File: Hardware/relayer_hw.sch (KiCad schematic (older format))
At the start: 18 parts

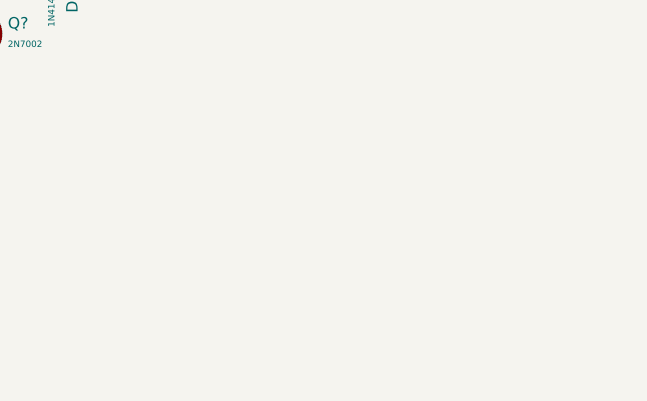
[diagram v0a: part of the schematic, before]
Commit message: Esquematico do regulador linear da fonte
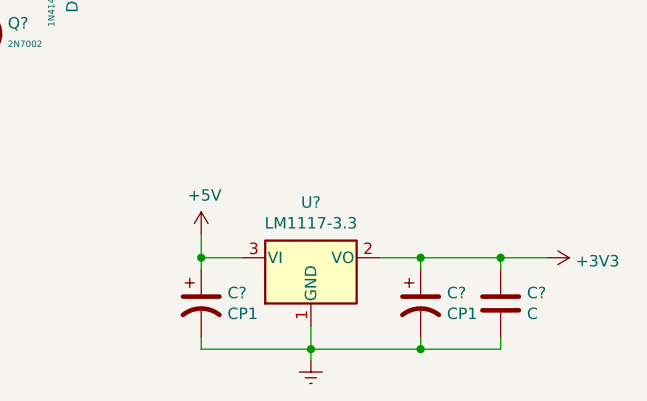
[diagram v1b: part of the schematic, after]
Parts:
- added C? (x2): CP1, symbol Device:CP1
- added C?: C, symbol Device:C
- added U?: LM1117-3.3, symbol Regulator_Linear:LM1117-3.3
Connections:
- wire segments 41 -> 57
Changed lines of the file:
@@
 	3390 5450 3390 5240
 Connection ~ 3390 5240
+$Comp
+L Regulator_Linear:LM1117-3.3 U?
+U 1 1 60667377
+P 3700 6690
+F 0 "U?" H 3700 6932 50  0000 C CNN
+F 1 "LM1117-3.3" H 3700 6841 50  0000 C CNN
+F 2 "" H 3700 6690 50  0001 C CNN
+F 3 "http://www.ti.com/lit/ds/symlink/lm1117.pdf" H 3700 6690 50  0001 C CNN
+	1    3700 6690
+	1    0    0    -1
+$EndComp
+$Comp
+L Device:CP1 C?
+U 1 1 60668957
+P 3220 6890
+F 0 "C?" H 3335 6936 50  0000 L CNN
+F 1 "CP1" H 3335 6845 50  0000 L CNN
+F 2 "" H 3220 6890 50  0001 C CNN
+F 3 "~" H 3220 6890 50  0001 C CNN
+	1    3220 6890
+	1    0    0    -1
+$EndComp
+$Comp
+L Device:CP1 C?
+U 1 1 60669A49
+P 4180 6890
+F 0 "C?" H 4295 6936 50  0000 L CNN
+F 1 "CP1" H 4295 6845 50  0000 L CNN
+F 2 "" H 4180 6890 50  0001 C CNN
+F 3 "~" H 4180 6890 50  0001 C CNN
+	1    4180 6890
+	1    0    0    -1
+$EndComp
+$Comp
+L Device:C C?
+U 1 1 6066C69B
+P 4530 6890
+F 0 "C?" H 4645 6936 50  0000 L CNN
+F 1 "C" H 4645 6845 50  0000 L CNN
+F 2 "" H 4568 6740 50  0001 C CNN
+F 3 "~" H 4530 6890 50  0001 C CNN
+	1    4530 6890
+	1    0    0    -1
+$EndComp
+Wire Wire Line
+	3220 6740 3220 6690
+Wire Wire Line
+	3220 6690 3400 6690
+Wire Wire Line
+	4000 6690 4180 6690
+Wire Wire Line
+	4180 6690 4180 6740
+Wire Wire Line
+	4530 6740 4530 6690
+Wire Wire Line
+	4530 6690 4180 6690
+Connection ~ 4180 6690
+Wire Wire Line
+	3220 7040 3220 7090
+Wire Wire Line
+	3220 7090 3700 7090
+Wire Wire Line
+	4180 7090 4180 7040
+Wire Wire Line
+	4530 7040 4530 7090
+Wire Wire Line
+	4530 7090 4180 7090
+Connection ~ 4180 7090
+Wire Wire Line
+	3700 6990 3700 7090
+Connection ~ 3700 7090
+Wire Wire Line
+	3700 7090 4180 7090
+$Comp
+L power:Earth #PWR?
+U 1 1 60672AE5
+P 3700 7140
+F 0 "#PWR?" H 3700 6890 50  0001 C CNN
+F 1 "Earth" H 3700 6990 50  0001 C CNN
+F 2 "" H 3700 7140 50  0001 C CNN
+F 3 "~" H 3700 7140 50  0001 C CNN
+	1    3700 7140
+	1    0    0    -1
+$EndComp
+Wire Wire Line
+	3700 7140 3700 7090
+$Comp
+L power:+3V3 #PWR?
+U 1 1 60674258
+P 4730 6690
+F 0 "#PWR?" H 4730 6540 50  0001 C CNN
+F 1 "+3V3" V 4745 6818 50  0000 L CNN
+F 2 "" H 4730 6690 50  0001 C CNN
+F 3 "" H 4730 6690 50  0001 C CNN
+	1    4730 6690
+	0    1    1    0
+$EndComp
+Wire Wire Line
+	4730 6690 4530 6690
+Connection ~ 4530 6690
+$Comp
+L power:+5V #PWR?
+U 1 1 60676AA9
+P 3220 6590
+F 0 "#PWR?" H 3220 6440 50  0001 C CNN
+F 1 "+5V" H 3235 6763 50  0000 C CNN
+F 2 "" H 3220 6590 50  0001 C CNN
+F 3 "" H 3220 6590 50  0001 C CNN
+	1    3220 6590
+	1    0    0    -1
+$EndComp
+Wire Wire Line
+	3220 6590 3220 6690
+Connection ~ 3220 6690
 $EndSCHEMATC

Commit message: Esquematico da fonte (não definitivo)
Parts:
- added C?: 220μF, symbol Device:CP1
- added C?: 100nF/275V, symbol Device:C
- added F?: Fuse, symbol Device:Fuse
- added L?: 10mH, symbol Device:L_Core_Iron_Coupled_Small
- added PS?: HLK-2M05, symbol Usr_Sym:HLK-2M05
- added RV?: Varistor_US, symbol Device:Varistor_US
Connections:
- wire segments 57 -> 68
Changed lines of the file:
@@
 L power:+3V3 #PWR?
 U 1 1 60674258
-P 4730 6690
-F 0 "#PWR?" H 4730 6540 50  0001 C CNN
-F 1 "+3V3" V 4745 6818 50  0000 L CNN
-F 2 "" H 4730 6690 50  0001 C CNN
-F 3 "" H 4730 6690 50  0001 C CNN
-	1    4730 6690
-	0    1    1    0
+P 4730 6590
+F 0 "#PWR?" H 4730 6440 50  0001 C CNN
+F 1 "+3V3" V 4745 6718 50  0000 L CNN
+F 2 "" H 4730 6590 50  0001 C CNN
+F 3 "" H 4730 6590 50  0001 C CNN
+	1    4730 6590
+	1    0    0    -1
 $EndComp
-Wire Wire Line
-	4730 6690 4530 6690
-Connection ~ 4530 6690
 $Comp
 L power:+5V #PWR?
@@
 	3220 6590 3220 6690
 Connection ~ 3220 6690
+$Comp
+L Usr_Sym:HLK-2M05 PS?
+U 1 1 60684E63
+P 2180 6870
+F 0 "PS?" H 2180 7175 50  0000 C CNN
+F 1 "HLK-2M05" H 2180 7084 50  0000 C CNN
+F 2 "" H 2180 7040 50  0001 C CNN
+F 3 "" H 2180 7040 50  0001 C CNN
+	1    2180 6870
+	1    0    0    -1
+$EndComp
+$Comp
+L Device:Fuse F?
+U 1 1 606867F7
+P 1000 6690
+F 0 "F?" V 803 6690 50  0000 C CNN
+F 1 "Fuse" V 894 6690 50  0000 C CNN
+F 2 "" V 930 6690 50  0001 C CNN
+F 3 "~" H 1000 6690 50  0001 C CNN
+	1    1000 6690
+	0    1    1    0
+$EndComp
+$Comp
+L Device:Varistor_US RV?
+U 1 1 60690A8A
+P 1220 6890
+F 0 "RV?" H 1323 6936 50  0000 L CNN
+F 1 "Varistor_US" H 1323 6845 50  0001 L CNN
+F 2 "" V 1150 6890 50  0001 C CNN
+F 3 "~" H 1220 6890 50  0001 C CNN
+	1    1220 6890
+	1    0    0    -1
+$EndComp
+$Comp
+L Device:CP1 C?
+U 1 1 606918D0
+P 2770 6890
+F 0 "C?" H 2885 6936 50  0000 L CNN
+F 1 "220μF" H 2885 6845 50  0000 L CNN
+F 2 "" H 2770 6890 50  0001 C CNN
+F 3 "~" H 2770 6890 50  0001 C CNN
+	1    2770 6890
+	1    0    0    -1
+$EndComp
+$Comp
+L Device:C C?
+U 1 1 60693778
+P 1550 6890
+F 0 "C?" H 1665 6936 50  0000 L CNN
+F 1 "100nF/275V" H 1665 6845 50  0001 L CNN
+F 2 "" H 1588 6740 50  0001 C CNN
+F 3 "~" H 1550 6890 50  0001 C CNN
+	1    1550 6890
+	1    0    0    -1
+$EndComp
+Wire Wire Line
+	2770 7040 2770 7090
+Wire Wire Line
+	2770 7090 3220 7090
+Connection ~ 3220 7090
+Wire Wire Line
+	2770 6740 2770 6690
+Wire Wire Line
+	2770 6690 3220 6690
+Wire Wire Line
+	2580 6790 2610 6790
+Wire Wire Line
+	2610 6790 2610 6690
+Wire Wire Line
+	2610 6690 2770 6690
+Connection ~ 2770 6690
+Wire Wire Line
+	2580 6990 2610 6990
+Wire Wire Line
+	2610 6990 2610 7090
+Wire Wire Line
+	2610 7090 2770 7090
+Connection ~ 2770 7090
+$Comp
+L Device:L_Core_Iron_Coupled_Small L?
+U 1 1 606BC58F
+P 1430 7580
+F 0 "L?" H 1430 7811 50  0000 C CNN
+F 1 "10mH" H 1430 7720 50  0000 C CNN
+F 2 "" H 1430 7580 50  0001 C CNN
+F 3 "~" H 1430 7580 50  0001 C CNN
+	1    1430 7580
+	1    0    0    -1
+$EndComp
+Wire Wire Line
+	4730 6590 4730 6690
+Wire Wire Line
+	4730 6690 4530 6690
+Connection ~ 4530 6690
 $EndSCHEMATC

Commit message: Simbolo do STM32WB55 e alimentação do chip (inicio)
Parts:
- added C?: 10μF, symbol Device:CP1
- added C?: 22μF, symbol Device:CP1
- added C? (x5): 100nF, symbol Device:C
- added C?: 220μF, symbol Device:CP1
- added C?: 100nF/275V, symbol Device:C
- added C? (x2): C, symbol Device:C
- added C? (x2): 4.7μF, symbol Device:C
- added F?: Fuse, symbol Device:Fuse
- added J? (x2): AC_IN, symbol Connector:Screw_Terminal_01x02
- added J?: AC_OUT, symbol Connector:Screw_Terminal_01x02
- added L?: 10mH, symbol Device:L_Core_Iron_Coupled_Small
- added PS?: HLK-2M05, symbol Usr_Sym:HLK-2M05
- added RV?: Varistor_US, symbol Device:Varistor_US
- added U?: LM1117-3.3, symbol Regulator_Linear:LM1117-3.3
- added U?: STM32WB55, symbol Usr_Sym:STM32WB55
- C?: value CP1 -> 10μF
- C?: value CP1 -> 22μF
- C?: value C -> 100nF
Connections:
- net labels added: GNDPWR, VDD, VDDSMPS, VFBSMPS, VLXSMPS
- wire segments 68 -> 198
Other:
- moved on the sheet: C?, D?, F?, PS?, Q?, R?, RLY?, RV?, U?

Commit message: Fonte definitiva/ LEDs sem mosfet driver/ Esquematico reorganizado/ Datasheets
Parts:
- removed C?: 100n, symbol Device:C
- removed C?: 10μF, symbol Device:CP1
- removed C?: 22μF, symbol Device:CP1
- removed C?: 100nF, symbol Device:C
- removed C?: 220μF, symbol Device:CP1
- removed C?: 100nF/275V, symbol Device:C
- removed C? (x2): C, symbol Device:C
- removed D? (x2): LED_ALT, symbol Device:LED_ALT
- removed F?: Fuse, symbol Device:Fuse
- removed J?: AC_IN, symbol Connector:Screw_Terminal_01x02
- removed L? (x2): 10mH, symbol Device:L_Core_Iron_Coupled_Small
- removed PS?: HLK-2M05, symbol Usr_Sym:HLK-2M05
- removed R? (x2): 100R, symbol Device:R_US
- removed R?: 1k, symbol Device:R_US
- removed R?: 150, symbol Device:R_US
- removed R? (x2): 150R, symbol Device:R_US
- removed R? (x2): 1M, symbol Device:R_US
- removed RV?: Varistor_US, symbol Device:Varistor_US
- removed SW?: SW_Push, symbol Switch:SW_Push
- removed U?: 2N7002DW-7-F, symbol Usr_Sym:2N7002DW-7-F
- removed U?: LM1117-3.3, symbol Regulator_Linear:LM1117-3.3
- added C?: 100nF, symbol Device:C
- added C?: 100pF, symbol Device:C
- added C? (x3): 100n, symbol Device:C
- added C? (x4): C, symbol Device:C
- added D?: Red_LED, symbol Device:LED_ALT
- added D?: Green_LED, symbol Device:LED_ALT
- added J?: STLink, symbol Connector_Generic:Conn_01x04
- added J?: BOOT0, symbol Connector_Generic:Conn_01x02
- added JP?: Wire, symbol Device:Jumper
- added L?: 10mH, symbol Device:L_Core_Iron_Coupled
- added R? (x2): R_US, symbol Device:R_US
- added R?: 1k, symbol Device:R_US
- added R?: 10k, symbol Device:R_US
- added R? (x2): 150R, symbol Device:R_US
- added SW?: NRST, symbol Switch:SW_Push
- added SW?: USR_SW, symbol Switch:SW_Push
- added Y?: Crystal_GND23, symbol Device:Crystal_GND24
- added Y?: Crystal, symbol Device:Crystal
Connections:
- net labels added: F, N, VBAT, VDDA, VDDRF, VDDUSB
- net labels removed: GNDPWR
- wire segments 198 -> 188
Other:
- moved on the sheet: C?, D?, F?, J?, PS?, Q?, R?, RLY?, RV?, U?

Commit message: Circuito RF/ Reorganização prática do hardware
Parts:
- added IPD?: MLPF-WB55-01E3, symbol Usr_Sym:MLPF-WB55-01E3
- added U?: 902-9040, symbol Usr_Sym:902-9040-fermbuddy
- added Z?: AN3359, symbol Usr_Sym:AN3359
- added Z?: R, symbol Device:R
- added Z? (x2): C, symbol Device:C
- C?: footprint (none) -> Capacitor_THT:C_Rect_L18.0mm_W6.0mm_P15.00mm_FKS3_FKP3
- J?: footprint (none) -> TerminalBlock:TerminalBlock_bornier-2_P5.08mm
- R? (x2): value R_US -> 750R
- RV?: footprint (none) -> Varistor:RV_Disc_D12mm_W6.1mm_P7.5mm
- U?: footprint (none) -> Package_TO_SOT_SMD:SOT-223
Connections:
- net at R?.1: now also U?.45 (PB5); no longer U?.28 (PB0)
- net at U?.17 (PA8): no longer R?.1
- net at U?.18 (PA9): no longer R?.1
- net at U?.21 (RF1): now also IPD?.3 (IN)
- net at U?.36 (PA10): now also R?.1
- net at U?.37 (PA11): now also R?.1
- new net: IPD?.1 (OUT), U?.1 (A)
- new net: U?.2 (B), Z?.1, Z?.2
- new net: U?.3 (GND), U?.5 (GND)
- new net: U?.4 (GND), U?.6 (GND)
- new net: Z?.1, Z?.1, Z?.1 (RF)
- new net: IPD?.2 (GND4), IPD?.4 (GND1), IPD?.5 (GND2), IPD?.6 (GND3)
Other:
- note added: "Decoupling Capacitors"
- note added: "Impedance Match Network"
- note added: "Low-pass filter\n"
- note added: "Neutral Conductor"
- note added: "Power Supply"
- note added: "RF Switch"
- note added: "WJ127-5.0-2P"
- moved on the sheet: C?, D?, F?, J?, JP?, L?, PS?, Q?, R?, RLY?, RV?, SW?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

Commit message: Associação de datasheets e footprints
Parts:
- C?: footprint (none) -> Usr_pretty_lib:CAPC1608X90
- C? (x7): footprint (none) -> Capacitor_SMD:C_0402_1005Metric
- C?: footprint (none) -> Capacitor_THT:CP_Radial_D5.0mm_P2.00mm
- C? (x2): footprint (none) -> Capacitor_SMD:C_0201_0603Metric
- C? (x3): value 100n -> 100nF; footprint (none) -> Capacitor_SMD:C_0402_1005Metric
- C?: value C -> 10pF; footprint (none) -> Capacitor_SMD:C_0402_1005Metric
- C?: value C -> 10pF
- C? (x2): value C -> 100nF; footprint (none) -> Capacitor_SMD:C_0402_1005Metric
- D?: footprint Diode_THT:D_DO-35_SOD27_P7.62mm_Horizontal -> Usr_pretty_lib:SODFL1608X70N
- F?: value Fuse -> JFC2410-0500TS; footprint (none) -> Fuse:Fuse_2010_5025Metric_Pad1.52x2.65mm_HandSolder
- J?: footprint (none) -> Connector_PinHeader_2.54mm:PinHeader_1x04_P2.54mm_Vertical
- J?: footprint (none) -> Connector_PinHeader_2.54mm:PinHeader_1x02_P2.54mm_Vertical
- Y?: footprint (none) -> Crystal:Crystal_SMD_2016-4Pin_2.0x1.6mm
- Y?: footprint (none) -> Crystal:Crystal_SMD_2012-2Pin_2.0x1.2mm_HandSoldering
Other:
- note added: "Impedance Matching Network"
- note removed: "Impedance Match Network"

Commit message: Annotate / ERC
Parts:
- added TP1: TestPoint, TestPoint:TestPoint_Loop_D2.54mm_Drill1.5mm_Beaded, symbol Connector:TestPoint
- added TP2, TP3: TestPoint, TestPoint:TestPoint_Pad_D1.0mm, symbol Connector:TestPoint
- C19: renamed from C?; footprint (none) -> Usr_pretty_lib:CAPC1608X90
- D2, D3: renamed from D?; footprint (none) -> LED_THT:LED_D5.0mm_Clear
- IPD1: renamed from IPD?; footprint (none) -> Usr_pretty_lib:SON160P500X500X140-6N
- L1: renamed from L?; footprint (none) -> Usr_pretty_lib:FL2D-Z5-103; symbol Device:L_Core_Iron_Coupled -> Usr_Sym:L_Core_Ferrite_Coupled
- PS1: renamed from PS?; footprint (none) -> Usr_pretty_lib:HLK-2M05
- R1, R2, R3, R4, R5, R6, R7, R8: renamed from R?; footprint (none) -> Resistor_SMD:R_0805_2012Metric_Pad1.15x1.40mm_HandSolder
- RLY1: renamed from RLY?; footprint (none) -> Usr_pretty_lib:HF32F-G 005-HS
- SW2: renamed from SW?; footprint (none) -> Button_Switch_THT:SW_PUSH_6mm_H13mm
- U1: renamed from U?; footprint (none) -> Usr_pretty_lib:QFN50P700X700X60-49N
- U2: renamed from U?; footprint (none) -> Usr_pretty_lib:902-9040
- Z1, Z2, Z3: renamed from Z?; footprint (none) -> Resistor_SMD:R_0402_1005Metric
- Z4: renamed from Z?; footprint (none) -> Usr_pretty_lib:AN3359_antenna
- gave numbers to parts that had none: 32
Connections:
- net VBAT is gone; now on net 3V3: C11.1, U1.1 (VBAT)
- net VDD is gone; now on net 3V3: C10.1, C5.1, C6.1, C8.1, U1.20 (VDD), U1.35 (VDD), U1.48 (VDD)
- net VDDA is gone; now on net 3V3: C9.1, U1.8 (VDDA~)
- net VDDRF is gone; now on net 3V3: C17.1, C18.1, U1.23 (VDDRF~)
- net VDDSMPS is gone; now on net 3V3: C12.1, C14.1, U1.31 (VFBSMPS), U1.33 (VLXSMPS), U1.34 (VDDSMPS)
- net VDDUSB is gone; now on net 3V3: C13.1, U1.40 (VDDUSB)
- net N: now also L1.2; no longer L1.3
- net 5V: now reaches D1.1 (K), RLY1.DC2
- net 5V: now also C15.1, C16.1, PS1.4 (+Vout), U3.3 (VI), TP2.1
- net 3V3: now reaches C19.1, C20.1, U3.2 (VO)
- net 3V3: now also TP3.1
- net at PS1.1 (AC1): now also L1.4; no longer L1.2
- net at PS1.2 (AC2): now also L1.3; no longer L1.4
- net at U1.17 (PA8): now also TP1.1
- no-connect marks 0 -> 22

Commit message: Correções de limites eletricos e remocao da pasta 'Datasheets'
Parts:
- RLY1: footprint Usr_pretty_lib:HF32F-G 005-HS -> Usr_pretty_lib:HF32F-G005-HS
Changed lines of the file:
@@
 Comp "Universidade Federal de Uberlândia"
 Comment1 "All datasheet links are in the components properties ;"
-Comment2 "Max. switching loads of 10A / 2500VA / 300W;"
+Comment2 "Max. switching loads of 3A / approx. 300W;"
 Comment3 "Device projected for home automation purposes;"
 Comment4 ""
@@
 F 0 "RLY1" H 1920 2405 50  0000 C CNN
 F 1 "HF32F-G_005-HS" H 1920 2314 50  0000 C CNN
-F 2 "Usr_pretty_lib:HF32F-G 005-HS" H 1920 2290 50  0001 C CNN
+F 2 "Usr_pretty_lib:HF32F-G005-HS" H 1920 2290 50  0001 C CNN
 F 3 "https://www.alldatasheet.com/datasheet-pdf/pdf/312373/HONGFA/HF32F-G.html" H 1920 2290 50  0001 C CNN
 	1    1920 2090
@@
 F 1 "JFC2410-0500TS" V 6404 1339 39  0000 L CNN
 F 2 "Fuse:Fuse_2010_5025Metric_Pad1.52x2.65mm_HandSolder" V 6440 1400 50  0001 C CNN
-F 3 "https://datasheet.lcsc.com/lcsc/1806130715_Littelfuse-0230-500MXP_C178894.pdf" H 6510 1400 50  0001 C CNN
+F 3 "https://datasheet.lcsc.com/lcsc/1809211427_Shenzhen-JDT-Fuse-JFC2410-0500TS_C136377.pdf" H 6510 1400 50  0001 C CNN
 	1    6510 1400
 	0    1    1    0
